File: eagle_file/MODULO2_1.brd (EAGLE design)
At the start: 129.5 x 87.6 mm, 59 parts, among them IC1 74HC595N

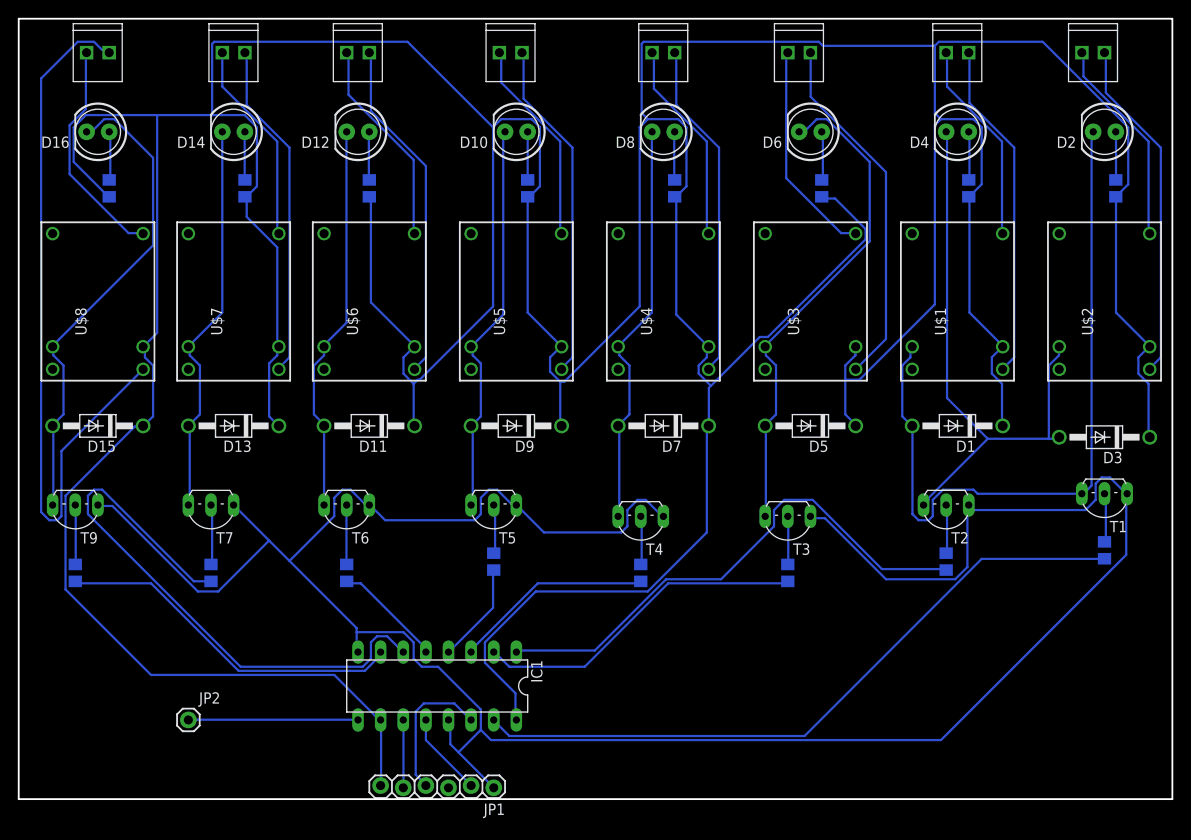
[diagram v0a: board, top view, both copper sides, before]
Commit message: Modulo 0 pdf
Modulo 0 senza contorno ai fori
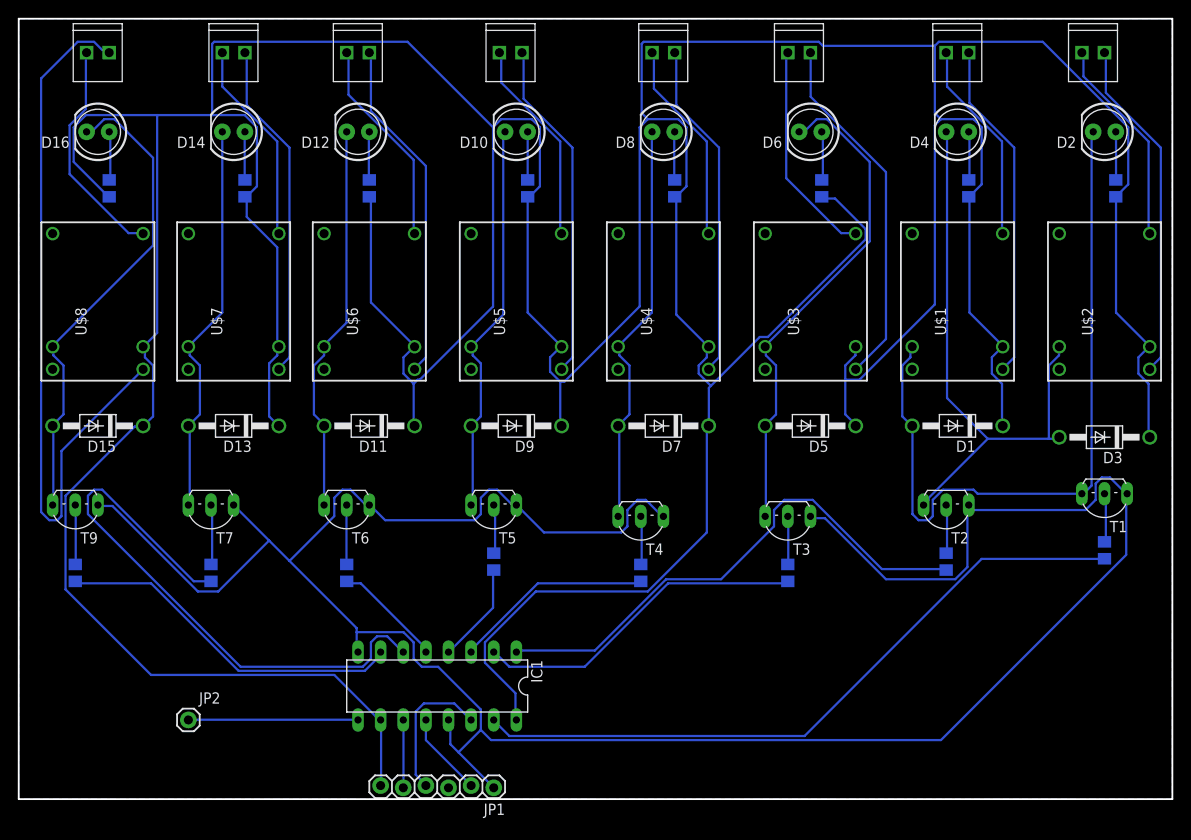
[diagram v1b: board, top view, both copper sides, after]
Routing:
- added copper zone on layer 16, net GND
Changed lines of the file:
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@@
 <layer number="19" name="Unrouted" color="6" fill="1" visible="yes" active="yes"/>
 <layer number="20" name="Dimension" color="15" fill="1" visible="yes" active="yes"/>
-<layer number="21" name="tPlace" color="7" fill="1" visible="yes" active="yes"/>
-<layer number="22" name="bPlace" color="7" fill="1" visible="yes" active="yes"/>
-<layer number="23" name="tOrigins" color="15" fill="1" visible="yes" active="yes"/>
-<layer number="24" name="bOrigins" color="15" fill="1" visible="yes" active="yes"/>
-<layer number="25" name="tNames" color="7" fill="1" visible="yes" active="yes"/>
-<layer number="26" name="bNames" color="7" fill="1" visible="yes" active="yes"/>
-<layer number="27" name="tValues" color="7" fill="1" visible="yes" active="yes"/>
-<layer number="28" name="bValues" color="7" fill="1" visible="yes" active="yes"/>
+<layer number="21" name="tPlace" color="7" fill="1" visible="no" active="yes"/>
+<layer number="22" name="bPlace" color="7" fill="1" visible="no" active="yes"/>
+<layer number="23" name="tOrigins" color="15" fill="1" visible="no" active="yes"/>
+<layer number="24" name="bOrigins" color="15" fill="1" visible="no" active="yes"/>
+<layer number="25" name="tNames" color="7" fill="1" visible="no" active="yes"/>
+<layer number="26" name="bNames" color="7" fill="1" visible="no" active="yes"/>
+<layer number="27" name="tValues" color="7" fill="1" visible="no" active="yes"/>
+<layer number="28" name="bValues" color="7" fill="1" visible="no" active="yes"/>
 <layer number="29" name="tStop" color="7" fill="3" visible="no" active="yes"/>
 <layer number="30" name="bStop" color="7" fill="6" visible="no" active="yes"/>
@@
 <layer number="37" name="tTest" color="7" fill="1" visible="no" active="yes"/>
 <layer number="38" name="bTest" color="7" fill="1" visible="no" active="yes"/>
-<layer number="39" name="tKeepout" color="4" fill="11" visible="yes" active="yes"/>
-<layer number="40" name="bKeepout" color="1" fill="11" visible="yes" active="yes"/>
-<layer number="41" name="tRestrict" color="4" fill="10" visible="yes" active="yes"/>
-<layer number="42" name="bRestrict" color="1" fill="10" visible="yes" active="yes"/>
-<layer number="43" name="vRestrict" color="2" fill="10" visible="yes" active="yes"/>
+<layer number="39" name="tKeepout" color="4" fill="11" visible="no" active="yes"/>
+<layer number="40" name="bKeepout" color="1" fill="11" visible="no" active="yes"/>
+<layer number="41" name="tRestrict" color="4" fill="10" visible="no" active="yes"/>
+<layer number="42" name="bRestrict" color="1" fill="10" visible="no" active="yes"/>
+<layer number="43" name="vRestrict" color="2" fill="10" visible="no" active="yes"/>
 <layer number="44" name="Drills" color="7" fill="1" visible="no" active="yes"/>
 <layer number="45" name="Holes" color="7" fill="1" visible="no" active="yes"/>
 <layer number="46" name="Milling" color="3" fill="1" visible="no" active="yes"/>
 <layer number="47" name="Measures" color="7" fill="1" visible="no" active="yes"/>
-<layer number="48" name="Document" color="7" fill="1" visible="yes" active="yes"/>
-<layer number="49" name="Reference" color="7" fill="1" visible="yes" active="yes"/>
+<layer number="48" name="Document" color="7" fill="1" visible="no" active="yes"/>
+<layer number="49" name="Reference" color="7" fill="1" visible="no" active="yes"/>
 <layer number="50" name="dxf" color="7" fill="1" visible="no" active="no"/>
-<layer number="51" name="tDocu" color="7" fill="1" visible="yes" active="yes"/>
-<layer number="52" name="bDocu" color="7" fill="1" visible="yes" active="yes"/>
+<layer number="51" name="tDocu" color="7" fill="1" visible="no" active="yes"/>
+<layer number="52" name="bDocu" color="7" fill="1" visible="no" active="yes"/>
 <layer number="53" name="tGND_GNDA" color="7" fill="9" visible="no" active="no"/>
 <layer number="54" name="bGND_GNDA" color="1" fill="9" visible="no" active="no"/>
@@
 <layer number="113" name="IDFDebug" color="4" fill="1" visible="no" active="yes"/>
 <layer number="116" name="Patch_BOT" color="9" fill="4" visible="no" active="yes"/>
-<layer number="118" name="Rect_Pads" color="7" fill="1" visible="yes" active="yes"/>
+<layer number="118" name="Rect_Pads" color="7" fill="1" visible="no" active="yes"/>
 <layer number="121" name="_tsilk" color="7" fill="1" visible="no" active="yes"/>
 <layer number="122" name="_bsilk" color="7" fill="1" visible="no" active="yes"/>
@@
 <layer number="127" name="_tValues" color="7" fill="1" visible="no" active="yes"/>
 <layer number="128" name="_bValues" color="7" fill="1" visible="no" active="yes"/>
-<layer number="129" name="Mask" color="7" fill="1" visible="yes" active="yes"/>
+<layer number="129" name="Mask" color="7" fill="1" visible="no" active="yes"/>
 <layer number="131" name="tAdjust" color="7" fill="1" visible="no" active="yes"/>
 <layer number="132" name="bAdjust" color="7" fill="1" visible="no" active="yes"/>
@@
 <layer number="223" name="223bmp" color="24" fill="1" visible="no" active="no"/>
 <layer number="224" name="224bmp" color="25" fill="1" visible="no" active="no"/>
-<layer number="225" name="225bmp" color="7" fill="1" visible="yes" active="yes"/>
-<layer number="226" name="226bmp" color="7" fill="1" visible="yes" active="yes"/>
-<layer number="227" name="227bmp" color="7" fill="1" visible="yes" active="yes"/>
-<layer number="228" name="228bmp" color="7" fill="1" visible="yes" active="yes"/>
-<layer number="229" name="229bmp" color="7" fill="1" visible="yes" active="yes"/>
-<layer number="230" name="230bmp" color="7" fill="1" visible="yes" active="yes"/>
-<layer number="231" name="231bmp" color="7" fill="1" visible="yes" active="yes"/>
+<layer number="225" name="225bmp" color="7" fill="1" visible="no" active="yes"/>
+<layer number="226" name="226bmp" color="7" fill="1" visible="no" active="yes"/>
+<layer number="227" name="227bmp" color="7" fill="1" visible="no" active="yes"/>
+<layer number="228" name="228bmp" color="7" fill="1" visible="no" active="yes"/>
+<layer number="229" name="229bmp" color="7" fill="1" visible="no" active="yes"/>
+<layer number="230" name="230bmp" color="7" fill="1" visible="no" active="yes"/>
+<layer number="231" name="231bmp" color="7" fill="1" visible="no" active="yes"/>
 <layer number="248" name="Housing" color="7" fill="1" visible="no" active="yes"/>
 <layer number="249" name="Edge" color="7" fill="1" visible="no" active="yes"/>
@@
 <layer number="251" name="SMDround" color="12" fill="11" visible="no" active="no"/>
 <layer number="254" name="cooling" color="7" fill="1" visible="no" active="yes"/>
-<layer number="255" name="routoute" color="7" fill="1" visible="yes" active="yes"/>
+<layer number="255" name="routoute" color="7" fill="1" visible="no" active="yes"/>
 </layers>
 <board>
@@
 <wire x1="51.8922" y1="7.7724" x2="53.0352" y2="6.6294" width="0.254" layer="16"/>
 <wire x1="124.3584" y1="34.29" x2="124.46" y2="34.29" width="0.254" layer="16"/>
+<polygon width="0.4064" layer="16">
+<vertex x="0" y="0"/>
+<vertex x="0" y="86.36"/>
+<vertex x="0" y="87.63"/>
+<vertex x="129.54" y="87.63"/>
+<vertex x="129.54" y="0"/>
+</polygon>
 </signal>
 <signal name="VCC">

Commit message: Fix Modulo 0
Pin all'esterno della scheda
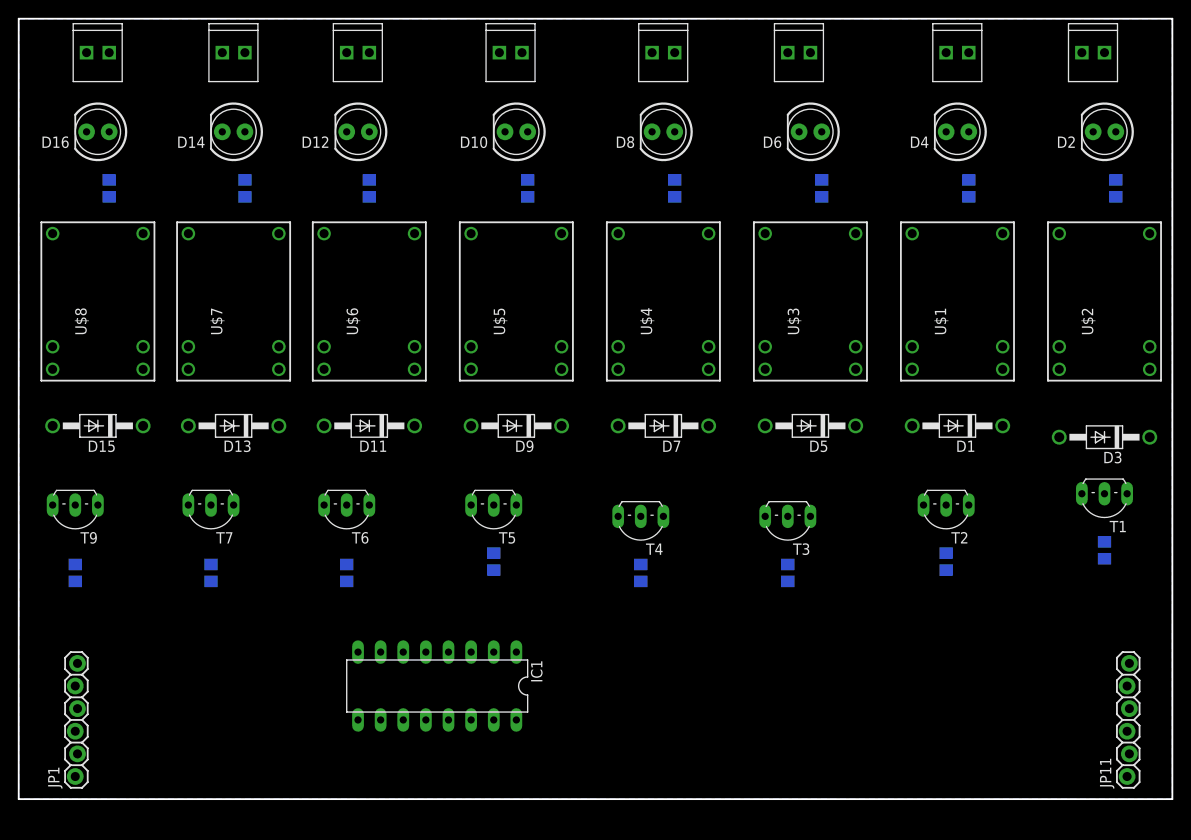
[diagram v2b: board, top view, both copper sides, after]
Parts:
- removed JP2: (no value), SparkFun-Connectors:1X01
- added JP11: (no value), SparkFun-Connectors:1X06_LOCK
- moved JP1 47.0 mm to (6.35, 2.54), turned to 90 degrees
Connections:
- removed net N$33: IC1.9, JP2.1
- new net QH: IC1.9, JP11.4
- net CS: now also JP11.2
- net GND: now also JP11.1
- net SCLK: now also JP11.5
- net SDI: now also JP11.3
- net VCC: now also JP11.6
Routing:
- net VCC: track 684.1 -> 0.00 mm
- net GND: track 276.4 -> 0.00 mm
- net N$3: track 83.1 -> 0.00 mm
- net N$48: track 81.7 -> 0.00 mm
- net N$1: track 77.6 -> 0.00 mm
- net N$31: track 66.2 -> 0.00 mm
- net N$6: track 65.8 -> 0.00 mm
- net N$2: track 59.7 -> 0.00 mm
- net N$7: track 56.2 -> 0.00 mm
- net N$26: track 54.5 -> 0.00 mm
- net N$10: track 46.0 -> 0.00 mm
- net N$23: track 44.8 -> 0.00 mm
- net N$17: track 44.7 -> 0.00 mm
- net N$20: track 43.9 -> 0.00 mm
- net N$38: track 40.5 -> 0.00 mm
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
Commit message: Modulo 2_2 pdf
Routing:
- net VCC: track 0.00 -> 745.2 mm
- net GND: track 0.00 -> 225.5 mm
- net SDI: track 0.00 -> 136.6 mm
- net N$23: track 0.00 -> 136.1 mm
- net SCLK: track 0.00 -> 133.8 mm
- net CS: track 0.00 -> 123.1 mm
- net N$3: track 0.00 -> 110.4 mm
- net N$34: track 0.00 -> 100.2 mm
- net QH: track 0.00 -> 89.2 mm
- net N$1: track 0.00 -> 77.3 mm
- net N$7: track 0.00 -> 74.0 mm
- net N$6: track 0.00 -> 67.2 mm
- net N$46: track 0.00 -> 60.2 mm
- net N$20: track 0.00 -> 57.1 mm
- net SDO: track 0.00 -> 52.8 mm
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
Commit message: Modulo 2_1
Modolo2_1.pdf per controllare i footprint
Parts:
- removed JP10: (no value), SparkFun-Connectors:1X02_2.54_SCREWTERM
- added JP2: (no value), SparkFun-Connectors:SCREWTERMINAL-3.5MM-3
- JP3, JP4, JP5, JP6, JP7, JP8, JP9: device SparkFun-Connectors:1X02_2.54_SCREWTERM -> SparkFun-Connectors:SCREWTERMINAL-3.5MM-3
- moved JP4 27.9 mm to (91.4, 83.8), turned to 180 degrees
- moved IC1 20.3 mm to (67.3, 12.7)
- moved JP3 19.7 mm to (123.8, 83.8), turned to 180 degrees
- moved JP1 15.3 mm to (17.8, 12.7), turned to 180 degrees
- moved JP6 13.3 mm to (57.8, 83.8), turned to 180 degrees
- moved JP7 12.7 mm to (41.3, 83.8), turned to 180 degrees
- moved JP9 12.1 mm to (10.8, 83.8), turned to 180 degrees
- moved JP5 12.1 mm to (74.3, 83.8), turned to 180 degrees
- moved JP8 10.8 mm to (26.0, 83.8), turned to 180 degrees
- moved JP11 10.5 mm to (121.9, 12.7), turned to 180 degrees
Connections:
- new net N$33: JP2.1, U$1.8
- new net N$50: JP7.3, U$6.7
- new net N$51: JP8.1, U$7.8
- new net N$52: JP8.2, U$7.14
- new net N$53: JP8.3, U$7.7
- new net N$54: JP9.1, U$8.8
- new net N$55: JP9.2, U$8.14
- new net N$56: JP9.3, U$8.7
- net N$34: now also JP2.2, U$1.14; no longer JP3.P1, U$1.8
- net N$35: now also JP2.3, U$1.7; no longer JP3.P2, U$1.14
- net N$36: now also JP3.1; no longer JP4.P1
- net N$37: now also JP3.2; no longer JP4.P2
- net N$38: now also JP3.3, U$2.7; no longer JP5.P1, U$3.8
- net N$39: now also JP4.1, U$3.8; no longer JP5.P2, U$3.14
- net N$40: now also JP4.2, U$3.14; no longer JP6.P1, U$4.8
- net N$41: now also JP4.3, U$3.7; no longer JP6.P2, U$4.14
- net N$42: now also JP5.1, U$4.8; no longer JP7.P1, U$5.8
- net N$43: now also JP5.2, U$4.14; no longer JP7.P2, U$5.14
- net N$44: now also JP5.3, U$4.7; no longer JP8.P1, U$6.8
- net N$45: now also JP6.1, U$5.8; no longer JP8.P2, U$6.14
- net N$46: now also JP6.2, U$5.14; no longer JP9.P1, U$7.8
- net N$47: now also JP6.3, U$5.7; no longer JP9.P2, U$7.14
- net N$48: now also JP7.1, U$6.8; no longer JP10.P1, U$8.8
- net N$49: now also JP7.2, U$6.14; no longer JP10.P2, U$8.14
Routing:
- net GND: track 225.5 -> 0.00 mm
- net SDI: track 136.6 -> 0.00 mm
- net N$23: track 136.1 -> 60.0 mm
- net N$34: track 100.2 -> 25.3 mm
- net N$33: track 0.00 -> 62.4 mm
- net N$51: track 0.00 -> 54.9 mm
- net N$28: track 50.2 -> 6.78 mm
- net N$54: track 0.00 -> 42.2 mm
- net N$50: track 0.00 -> 38.3 mm
- net N$53: track 0.00 -> 38.3 mm
- net N$56: track 0.00 -> 37.5 mm
- net N$45: track 23.6 -> 59.8 mm
- net N$46: track 60.2 -> 26.0 mm
- net SCLK: track 133.8 -> 167.4 mm
- net N$49: track 23.1 -> 53.2 mm
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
